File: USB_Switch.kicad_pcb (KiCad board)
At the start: 2 copper layers, 38.1 x 63.5 mm, 30 parts, among them J1 Conn_01x06, J2 USB_IN, J3 USB_OUT, J4 Conn_01x08, J5 USB_OUT, Q1 Q_NMOS_GDS, Q2 Q_NMOS_GDS, SW1 PRGM, U1 AMS1117-3.3, U2 INA219AxD, U3 INA219AxD, U4 ESP-12F

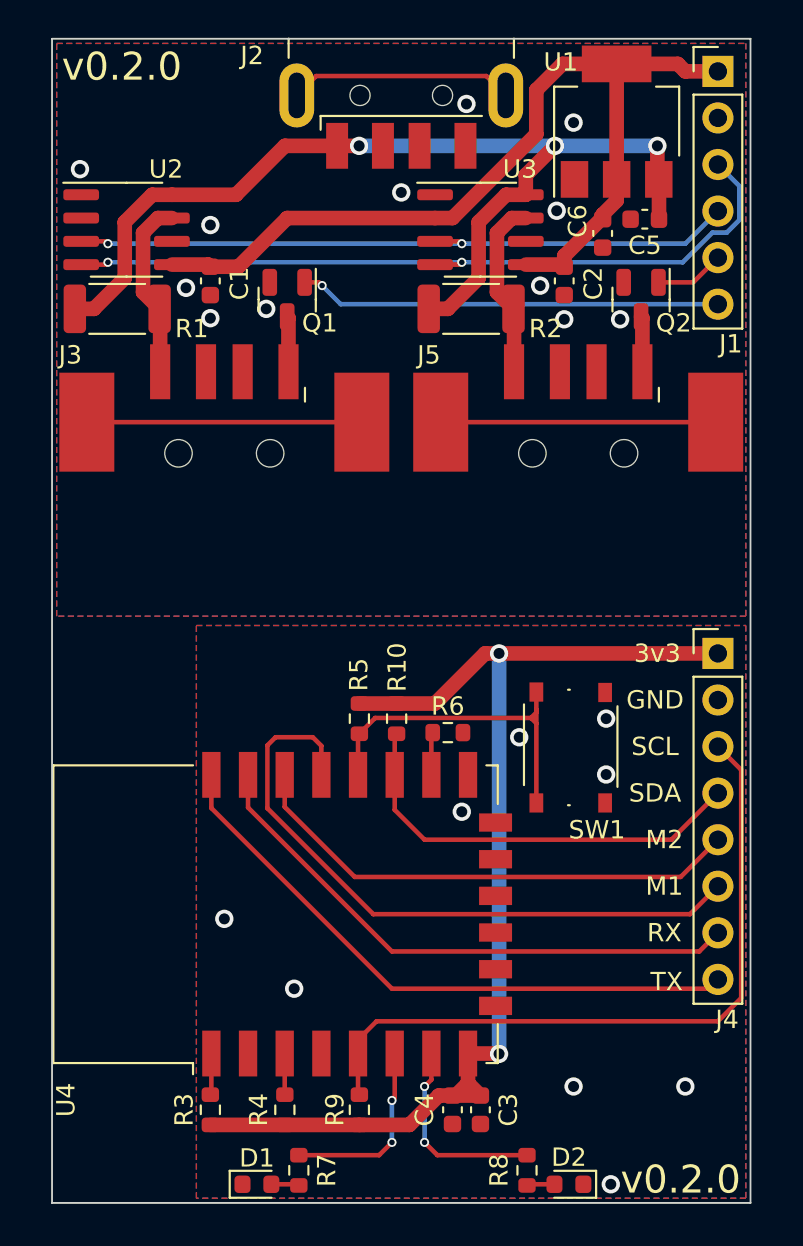
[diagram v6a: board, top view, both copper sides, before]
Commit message: Added note about copper pour on control board, added cutout on PCB behind antenna.
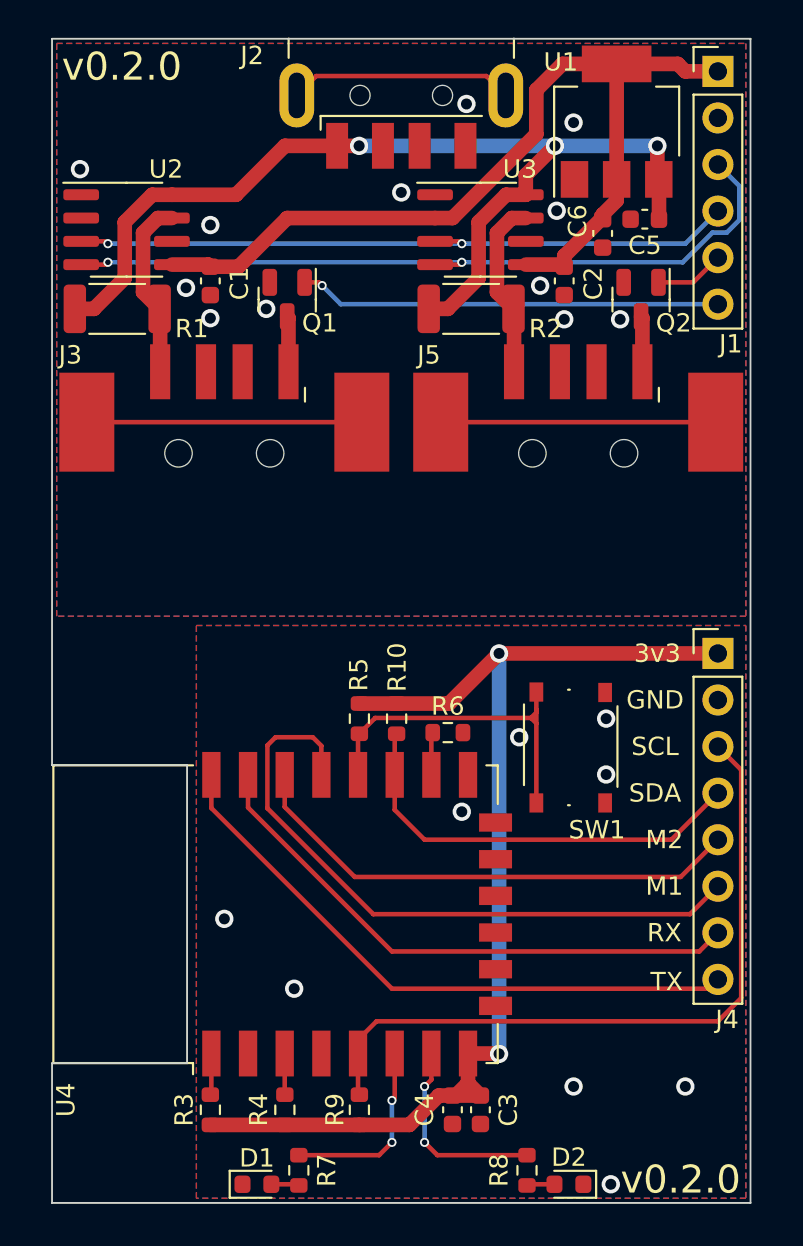
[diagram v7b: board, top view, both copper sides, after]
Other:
- outline, holes or cut-outs redrawn
- board text added: "Pull copper back entirely to avoid antenna area"
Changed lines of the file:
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@@
   )
   (gr_line locked (start 122.428 95.25) (end 169.672 95.25) (layer "Eco1.User") (width 0.1))
-  (gr_rect locked (start 127 63.5) (end 165.1 127) (layer "Edge.Cuts") (width 0.1) (fill none))
+  (gr_line (start 165.1 127) (end 127 127) (layer "Edge.Cuts") (width 0.1))
+  (gr_line (start 134.366 103.124) (end 127 103.124) (layer "Edge.Cuts") (width 0.1))
+  (gr_line (start 165.1 127) (end 165.1 63.5) (layer "Edge.Cuts") (width 0.1))
+  (gr_line (start 127 119.38) (end 134.366 119.38) (layer "Edge.Cuts") (width 0.1))
+  (gr_line (start 134.366 103.124) (end 134.366 119.38) (layer "Edge.Cuts") (width 0.1))
+  (gr_line (start 127 63.5) (end 165.1 63.5) (layer "Edge.Cuts") (width 0.1))
+  (gr_line (start 127 127) (end 127 119.38) (layer "Edge.Cuts") (width 0.1))
+  (gr_line (start 127 103.124) (end 127 63.5) (layer "Edge.Cuts") (width 0.1))
   (gr_text "SCL" (at 160.02 70.358) (layer "B.SilkS")
     (effects (font (size 1 1) (thickness 0.15)) (justify mirror))
@@
   )
   (gr_text "RX" (at 160.401 112.268) (layer "F.SilkS")
+    (effects (font (size 1 1) (thickness 0.15)))
+  )
+  (gr_text "Pull copper back entirely\nto avoid antenna area" (at 124.714 111.252 90) (layer "Cmts.User")
     (effects (font (size 1 1) (thickness 0.15)))
   )
@@
   (segment (start 162.814 115.316) (end 163.322 114.808) (width 0.25) (layer "F.Cu") (net 22))
   (segment (start 135.692 105.466) (end 145.542 115.316) (width 0.25) (layer "F.Cu") (net 22))
-  (segment (start 150.622 97.028) (end 147.891 99.759) (width 0.8) (layer "F.Cu") (net 23))
   (segment (start 148.095 121.145) (end 146.495 122.745) (width 0.8) (layer "F.Cu") (net 23))
   (segment (start 149.692 118.852) (end 149.692 120.469) (width 0.8) (layer "F.Cu") (net 23))
-  (segment (start 147.891 99.759) (end 143.764 99.759) (width 0.8) (layer "F.Cu") (net 23))
   (segment (start 148.844 121.145) (end 149.016 121.145) (width 0.8) (layer "F.Cu") (net 23))
   (segment (start 148.844 121.145) (end 150.368 121.145) (width 0.8) (layer "F.Cu") (net 23))
   (segment (start 146.495 122.745) (end 143.764 122.745) (width 0.8) (layer "F.Cu") (net 23))
   (segment (start 149.016 121.145) (end 149.692 120.469) (width 0.8) (layer "F.Cu") (net 23))
-  (segment (start 151.384 97.028) (end 150.622 97.028) (width 0.8) (layer "F.Cu") (net 23))
+  (segment (start 148.653 99.759) (end 143.764 99.759) (width 0.8) (layer "F.Cu") (net 23))
   (segment (start 149.692 118.852) (end 151.364 118.852) (width 0.8) (layer "F.Cu") (net 23))
   (segment (start 148.844 121.145) (end 148.095 121.145) (width 0.8) (layer "F.Cu") (net 23))
@@
   (segment (start 149.692 120.469) (end 150.368 121.145) (width 0.8) (layer "F.Cu") (net 23))
   (segment (start 151.364 118.852) (end 151.384 118.872) (width 0.8) (layer "F.Cu") (net 23))
+  (segment (start 151.384 97.028) (end 148.653 99.759) (width 0.8) (layer "F.Cu") (net 23))
   (via (at 151.384 97.028) (size 1) (drill 0.6) (layers "F.Cu" "B.Cu") (net 23))
   (via (at 151.384 118.872) (size 1) (drill 0.6) (layers "F.Cu" "B.Cu") (net 23))

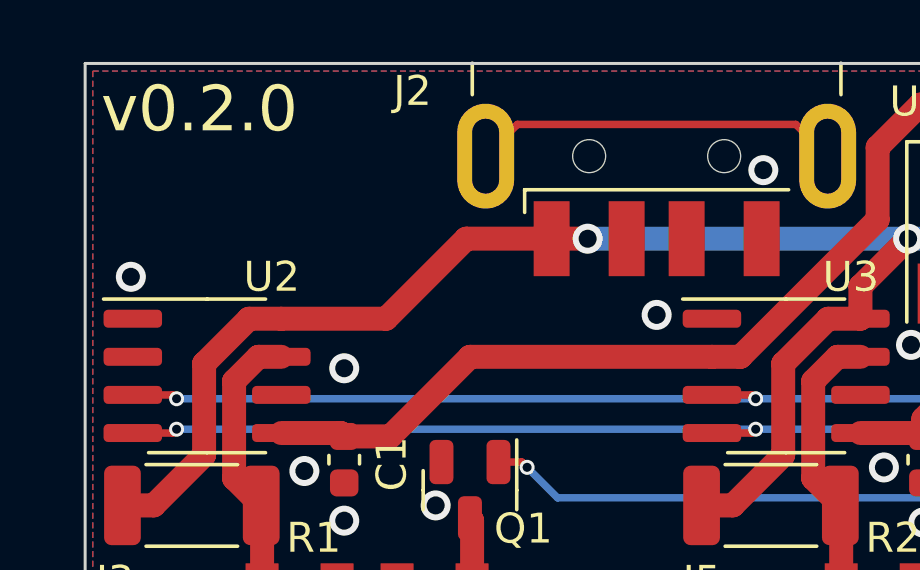
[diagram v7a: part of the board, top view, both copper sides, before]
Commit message: Added resistor between D+ and D-
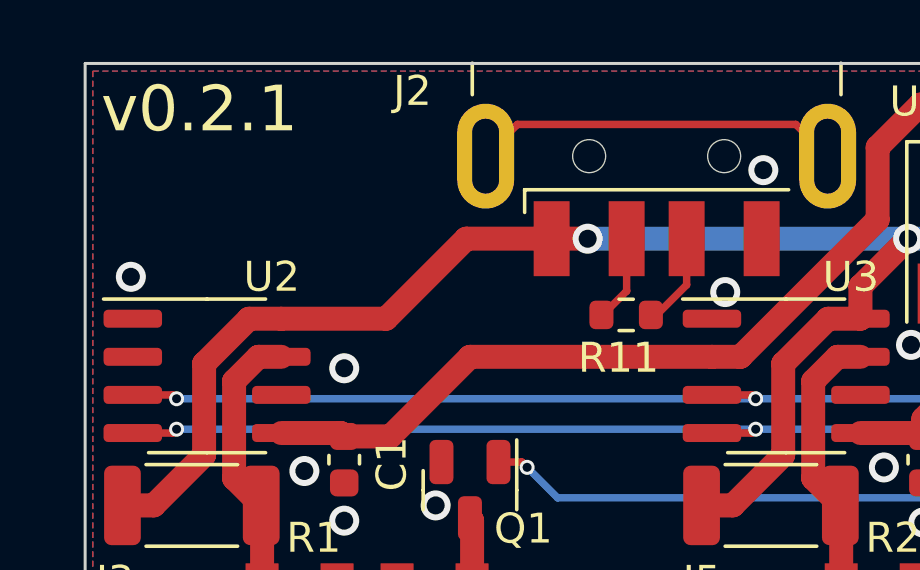
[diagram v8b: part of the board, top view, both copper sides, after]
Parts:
- added R11: 100, Resistor_SMD:R_0603_1608Metric, F.Cu at (145.0, 71.9)
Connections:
- J2 pad 2: unconnected-(J2-Pad2) -> Net-(J2-Pad2)
- J2 pad 3: unconnected-(J2-Pad3) -> Net-(J2-Pad3)
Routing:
- net Net-(J2-Pad3): track 0.00 -> 3.15 mm
- net Net-(J2-Pad2): track 0.00 -> 2.92 mm
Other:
- board text added: "v0.2.1"
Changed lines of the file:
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@@
   (net 30 "/MOSFET Board/M2_TOGGLE")
   (net 31 "/MOSFET Board/M1_TOGGLE")
-  (net 32 "unconnected-(J2-Pad2)")
-  (net 33 "unconnected-(J2-Pad3)")
+  (net 32 "Net-(J2-Pad2)")
+  (net 33 "Net-(J2-Pad3)")
   (net 34 "unconnected-(J2-Pad5)")
   (net 35 "unconnected-(J3-Pad2)")
@@
     (pad "2" smd roundrect (at 0.825 0 270) (size 0.8 0.95) (layers "F.Cu" "F.Paste" "F.Mask") (roundrect_rratio 0.25)
       (net 8 "Net-(D1-Pad2)") (pintype "passive"))
+    (model "${KICAD6_3DMODEL_DIR}/Resistor_SMD.3dshapes/R_0603_1608Metric.wrl"
+      (offset (xyz 0 0 0))
+      (scale (xyz 1 1 1))
+      (rotate (xyz 0 0 0))
+    )
+  )
+  (footprint "Resistor_SMD:R_0603_1608Metric" (layer "F.Cu")
+    (at 145.034 71.882 180)
+    (descr "Resistor SMD 0603 (1608 Metric), square (rectangular) end terminal, IPC_7351 nominal, (Body size source: IPC-SM-782 page 72, https://www.pcb-3d.com/wordpress/wp-content/uploads/ipc-sm-782a_amendment_1_and_2.pdf), generated with kicad-footprint-generator")
+    (tags "resistor")
+    (property "LCSC Part Number" "C22775")
+    (property "Manufacturer" "UNI-ROYAL(Uniroyal Elec)")
+    (property "Manufacturer Part Number" "0603WAF1000T5E")
+    (property "Sheetfile" "board_mosfet.kicad_sch")
+    (property "Sheetname" "MOSFET Board")
+    (attr smd)
+    (fp_text reference "R11" (at 0.254 -1.43) (layer "F.SilkS")
+      (effects (font (size 1 1) (thickness 0.15)))
+    )
+    (fp_text value "100" (at 0 1.43) (layer "F.Fab")
+      (effects (font (size 1 1) (thickness 0.15)))
+    )
+    (fp_text user "${REFERENCE}" (at 0 0) (layer "F.Fab")
+      (effects (font (size 0.4 0.4) (thickness 0.06)))
+    )
+    (fp_line (start -0.237258 -0.5225) (end 0.237258 -0.5225) (layer "F.SilkS") (width 0.12))
+    (fp_line (start -0.237258 0.5225) (end 0.237258 0.5225) (layer "F.SilkS") (width 0.12))
+    (fp_line (start -1.48 -0.73) (end 1.48 -0.73) (layer "F.CrtYd") (width 0.05))
+    (fp_line (start -1.48 0.73) (end -1.48 -0.73) (layer "F.CrtYd") (width 0.05))
+    (fp_line (start 1.48 0.73) (end -1.48 0.73) (layer "F.CrtYd") (width 0.05))
+    (fp_line (start 1.48 -0.73) (end 1.48 0.73) (layer "F.CrtYd") (width 0.05))
+    (fp_line (start 0.8 0.4125) (end -0.8 0.4125) (layer "F.Fab") (width 0.1))
+    (fp_line (start -0.8 -0.4125) (end 0.8 -0.4125) (layer "F.Fab") (width 0.1))
+    (fp_line (start -0.8 0.4125) (end -0.8 -0.4125) (layer "F.Fab") (width 0.1))
+    (fp_line (start 0.8 -0.4125) (end 0.8 0.4125) (layer "F.Fab") (width 0.1))
+    (pad "1" smd roundrect (at -0.825 0 180) (size 0.8 0.95) (layers "F.Cu" "F.Paste" "F.Mask") (roundrect_rratio 0.25)
+      (net 33 "Net-(J2-Pad3)") (pintype "passive"))
+    (pad "2" smd roundrect (at 0.825 0 180) (size 0.8 0.95) (layers "F.Cu" "F.Paste" "F.Mask") (roundrect_rratio 0.25)
+      (net 32 "Net-(J2-Pad2)") (pintype "passive"))
     (model "${KICAD6_3DMODEL_DIR}/Resistor_SMD.3dshapes/R_0603_1608Metric.wrl"
       (offset (xyz 0 0 0))
@@
       (net 4 "Net-(R3-Pad2)") (pinfunction "~{RST}") (pintype "input"))
     (pad "2" smd rect (at -7.6 -1.5 90) (size 2.5 1) (layers "F.Cu" "F.Paste" "F.Mask")
-      (net 11 "unconnected-(U4-Pad2)") (pinfunction "ADC") (pintype "input"))
+      (net 11 "unconnected-(U4-Pad2)") (pinfunction "ADC") (pintype "input+no_connect"))
     (pad "3" smd rect (at -7.6 0.5 90) (size 2.5 1) (layers "F.Cu" "F.Paste" "F.Mask")
       (net 5 "Net-(R4-Pad2)") (pinfunction "EN") (pintype "input"))
     (pad "4" smd rect (at -7.6 2.5 90) (size 2.5 1) (layers "F.Cu" "F.Paste" "F.Mask")
-      (net 12 "unconnected-(U4-Pad4)") (pinfunction "GPIO16") (pintype "bidirectional"))
+      (net 12 "unconnected-(U4-Pad4)") (pinfunction "GPIO16") (pintype "bidirectional+no_connect"))
     (pad "5" smd rect (at -7.6 4.5 90) (size 2.5 1) (layers "F.Cu" "F.Paste" "F.Mask")
       (net 24 "/Control Board/C_I2C_SCL") (pinfunction "GPIO14") (pintype "bidirectional"))
@@
       (net 10 "/MOSFET Board/5V_IN") (pinfunction "VBUS") (pintype "power_in"))
     (pad "2" smd rect (at -9.65 -1 90) (size 2.5 1.2) (layers "F.Cu" "F.Paste" "F.Mask")
-      (net 32 "unconnected-(J2-Pad2)") (pinfunction "D-") (pintype "bidirectional+no_connect"))
+      (net 32 "Net-(J2-Pad2)") (pinfunction "D-") (pintype "bidirectional"))
     (pad "3" smd rect (at -9.65 1 90) (size 2.5 1.2) (layers "F.Cu" "F.Paste" "F.Mask")
-      (net 33 "unconnected-(J2-Pad3)") (pinfunction "D+") (pintype "bidirectional+no_connect"))
+      (net 33 "Net-(J2-Pad3)") (pinfunction "D+") (pintype "bidirectional"))
     (pad "4" smd rect (at -9.65 3.5 90) (size 2.5 1.2) (layers "F.Cu" "F.Paste" "F.Mask")
       (net 27 "GND") (pinfunction "GND") (pintype "power_in"))
@@
     (effects (font (size 1 1) (thickness 0.15)))
   )
-  (gr_text "v0.2.0" (at 130.81 65.024) (layer "F.SilkS")
+  (gr_text "v0.2.1" (at 130.81 65.024) (layer "F.SilkS")
     (effects (font (size 1.524 1.524) (thickness 0.254)))
   )
@@
   (via (at 138.684 78.232) (size 1) (drill 0.6) (layers "F.Cu" "B.Cu") (net 27))
   (via (at 149.606 67.056) (size 1) (drill 0.6) (layers "F.Cu" "B.Cu") (net 27))
-  (via (at 146.05 71.882) (size 1) (drill 0.6) (layers "F.Cu" "B.Cu") (net 27))
+  (via (at 148.336 71.12) (size 1) (drill 0.6) (layers "F.Cu" "B.Cu") (net 27))
   (via (at 140.208 115.316) (size 1) (drill 0.6) (layers "F.Cu" "B.Cu") (net 27))
   (via (at 157.226 100.584) (size 1) (drill 0.6) (layers "F.Cu" "B.Cu") (net 27))
@@
   (segment (start 141.732 76.962) (end 142.748 77.978) (width 0.25) (layer "B.Cu") (net 31))
   (segment (start 142.748 77.978) (end 163.322 77.978) (width 0.25) (layer "B.Cu") (net 31))
+  (segment (start 145.05 71.088) (end 145.05 69.34) (width 0.25) (layer "F.Cu") (net 32))
+  (segment (start 144.256 71.882) (end 145.05 71.088) (width 0.25) (layer "F.Cu") (net 32))
+  (segment (start 144.209 71.882) (end 144.256 71.882) (width 0.25) (layer "F.Cu") (net 32))
+  (segment (start 147.05 70.882) (end 147.05 69.34) (width 0.25) (layer "F.Cu") (net 33))
+  (segment (start 146.05 71.882) (end 147.05 70.882) (width 0.25) (layer "F.Cu") (net 33))
+  (segment (start 145.859 71.882) (end 146.05 71.882) (width 0.25) (layer "F.Cu") (net 33))
   (segment (start 140.35 66.59) (end 141.408 65.532) (width 0.25) (layer "F.Cu") (net 34))
   (segment (start 150.692 65.532) (end 151.75 66.59) (width 0.25) (layer "F.Cu") (net 34))
